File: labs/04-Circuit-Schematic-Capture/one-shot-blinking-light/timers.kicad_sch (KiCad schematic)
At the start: 11 parts, among them U201 LM556

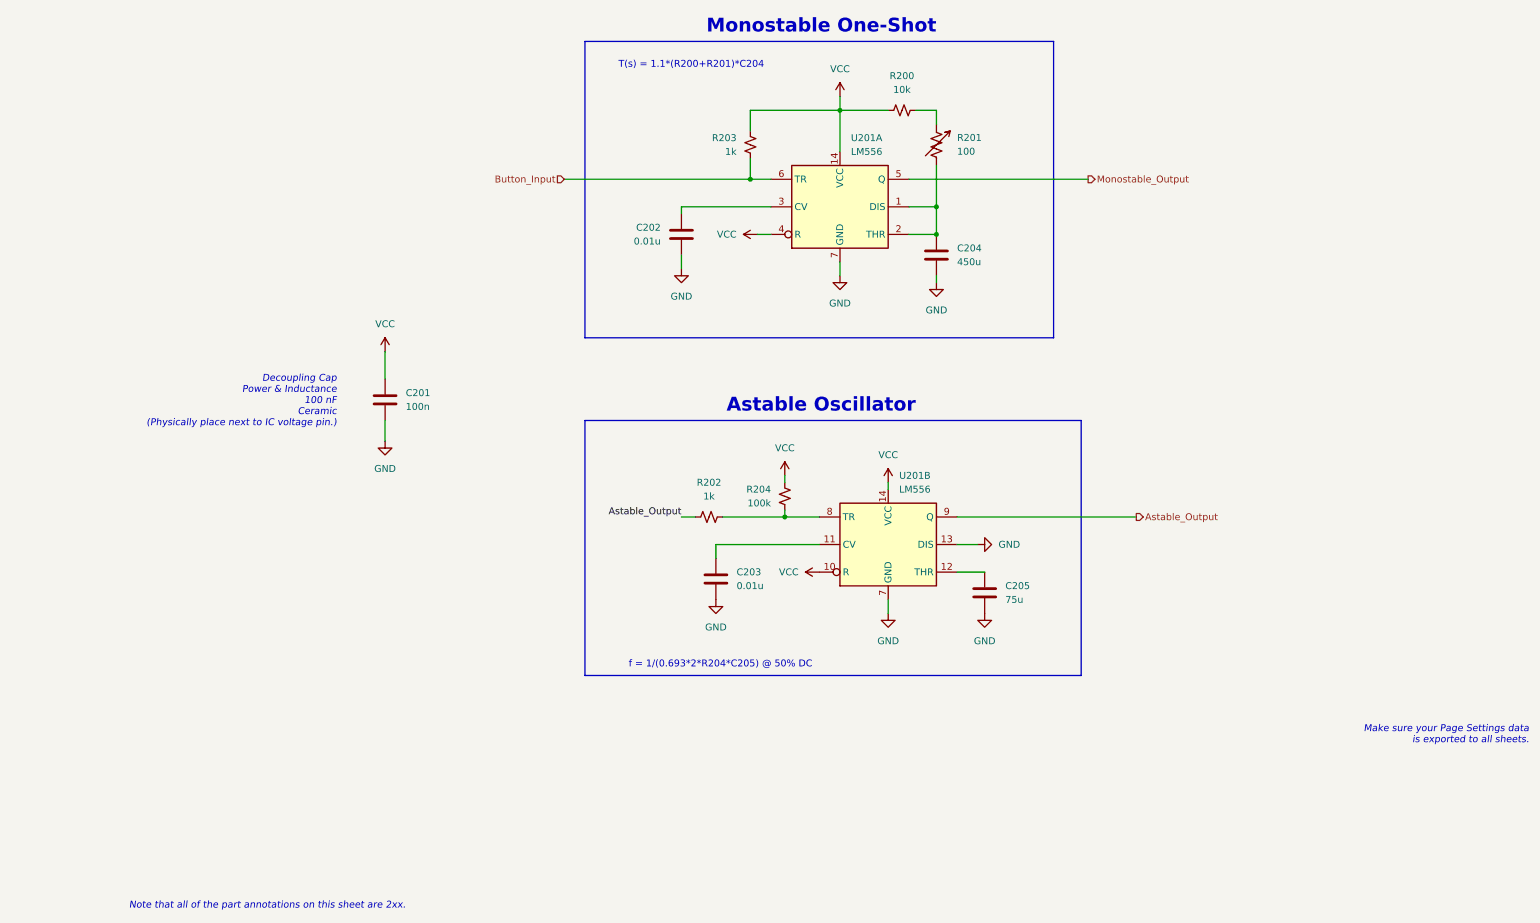
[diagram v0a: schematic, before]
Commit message: exclude mounting holes from BOM; add more annotation
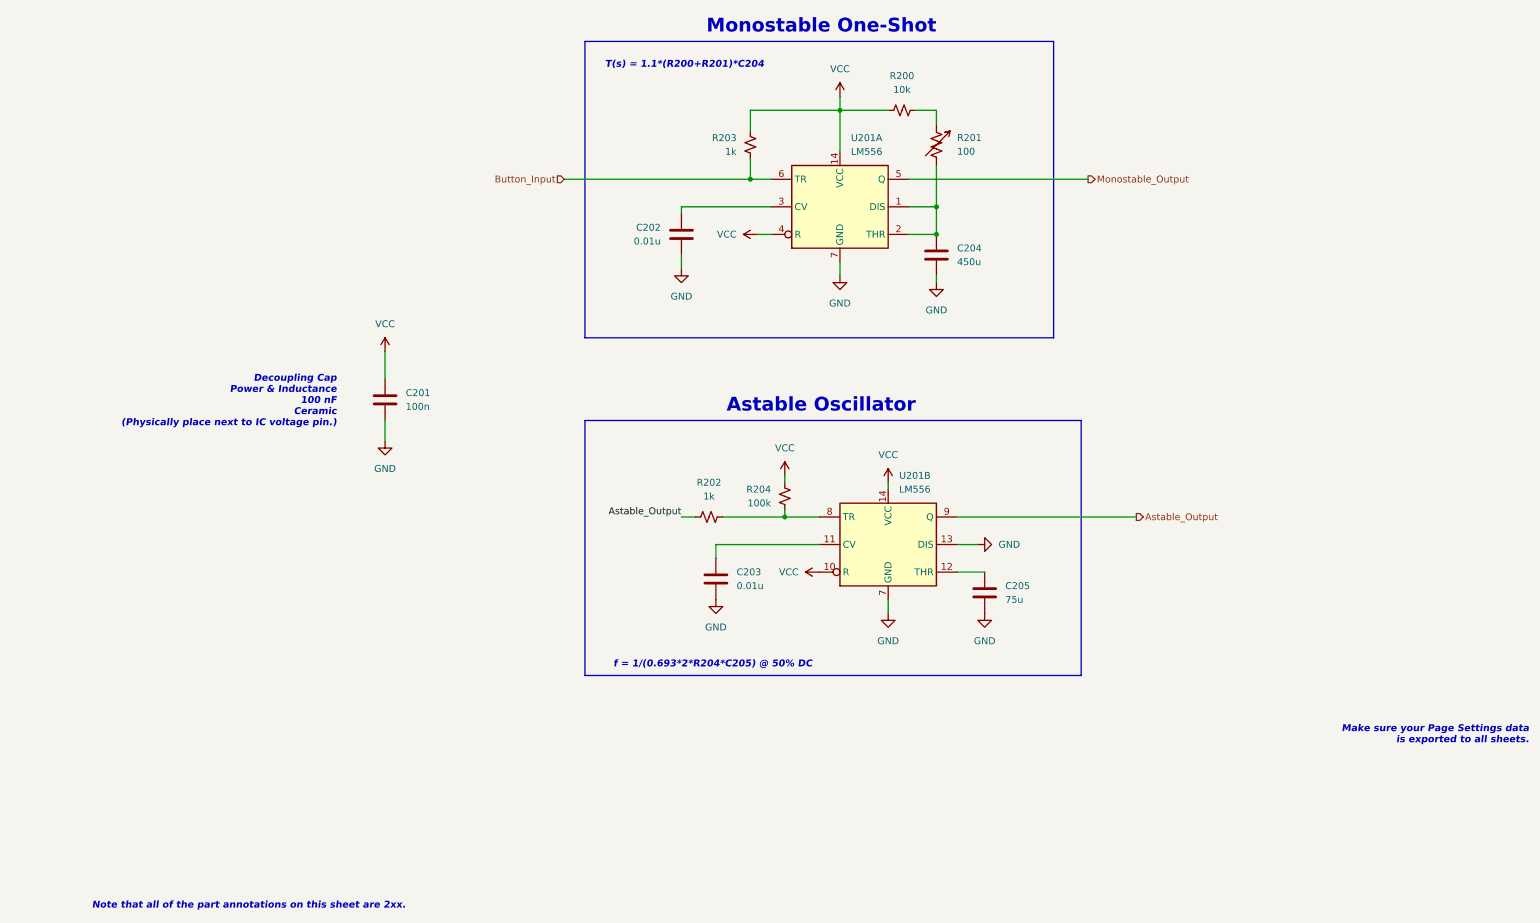
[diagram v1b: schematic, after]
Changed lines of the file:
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@@
   )
   (text "f = 1/(0.693*2*R204*C205) @ 50% DC" (at 148.59 149.86 180)
-    (effects (font (size 1.27 1.27)) (justify right bottom))
+    (effects (font (size 1.27 1.27) (thickness 0.254) bold italic) (justify right bottom))
   )
   (text "Monostable One-Shot" (at 171.45 33.02 180)
@@
   (text "Decoupling Cap\nPower & Inductance\n100 nF\nCeramic\n(Physically place next to IC voltage pin.)"
     (at 60.96 105.41 180)
-    (effects (font (size 1.27 1.27) italic) (justify right bottom))
+    (effects (font (size 1.27 1.27) (thickness 0.254) bold italic) (justify right bottom))
   )
   (text "T(s) = 1.1*(R200+R201)*C204" (at 139.7 39.37 180)
-    (effects (font (size 1.27 1.27)) (justify right bottom))
+    (effects (font (size 1.27 1.27) (thickness 0.254) bold italic) (justify right bottom))
   )
   (text "Make sure your Page Settings data\nis exported to all sheets."
     (at 280.67 163.83 180)
-    (effects (font (size 1.27 1.27) italic) (justify right bottom))
+    (effects (font (size 1.27 1.27) (thickness 0.254) bold italic) (justify right bottom))
   )
   (text "Note that all of the part annotations on this sheet are 2xx."
     (at 73.66 194.31 180)
-    (effects (font (size 1.27 1.27) italic) (justify right bottom))
+    (effects (font (size 1.27 1.27) (thickness 0.254) bold italic) (justify right bottom))
   )
   (label "Astable_Output" (at 124.46 121.92 180)
